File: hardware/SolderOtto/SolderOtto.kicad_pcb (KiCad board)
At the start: 2 copper layers, 102 x 80 mm, 179 parts, among them J201 Conn_02x04_Counter_Clockwise, J301 TC-2050, J401 Conn_01x20, J601 Conn_01x07, Q201 T2N7002AK, Q202 BC858B, Q203 BC847A, Q204 BC847A, Q701 BC847A, Q702 BC858B, Q703 BC847A, Q801 Q_Dual_NMOS, Q802 Q_Dual_NMOS, Q803 DTD123EK, Q804 DTD123EK, Q805 Q_Dual_NMOS, Q806 Q_Dual_NMOS, Q807 DTD123EK, Q808 DTD123EK, U201 LM5012, U202 AP3211K, U203 AP3211K, U204 AP3211K, U205 LM27761, U206 MCP9701T-E/TT, U301 STM32L496RGTx, U501 SN74LVC2G125, U701 OP07, U702 LM358, U703 74hc4053, U704 OP07, U705 OP07, U801 VOM1271, U802 VOM1271, U803 VOM1271, U804 VOM1271, Y301 Crystal

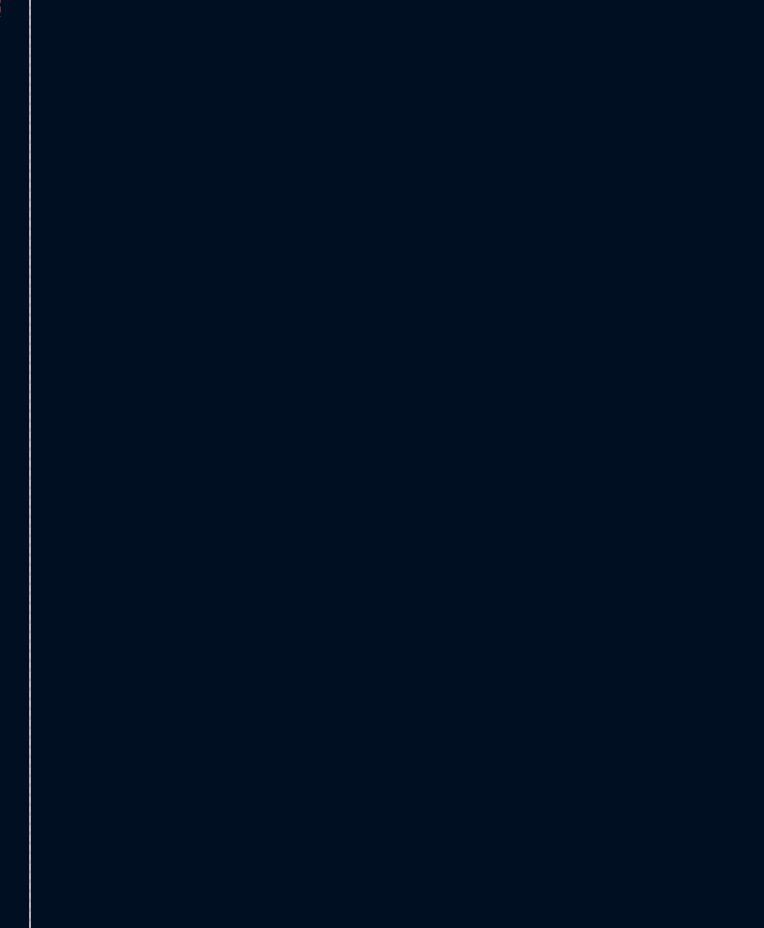
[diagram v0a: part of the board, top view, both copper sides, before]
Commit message: add support for tweezers AM-120
change mcu to stm32h573VI
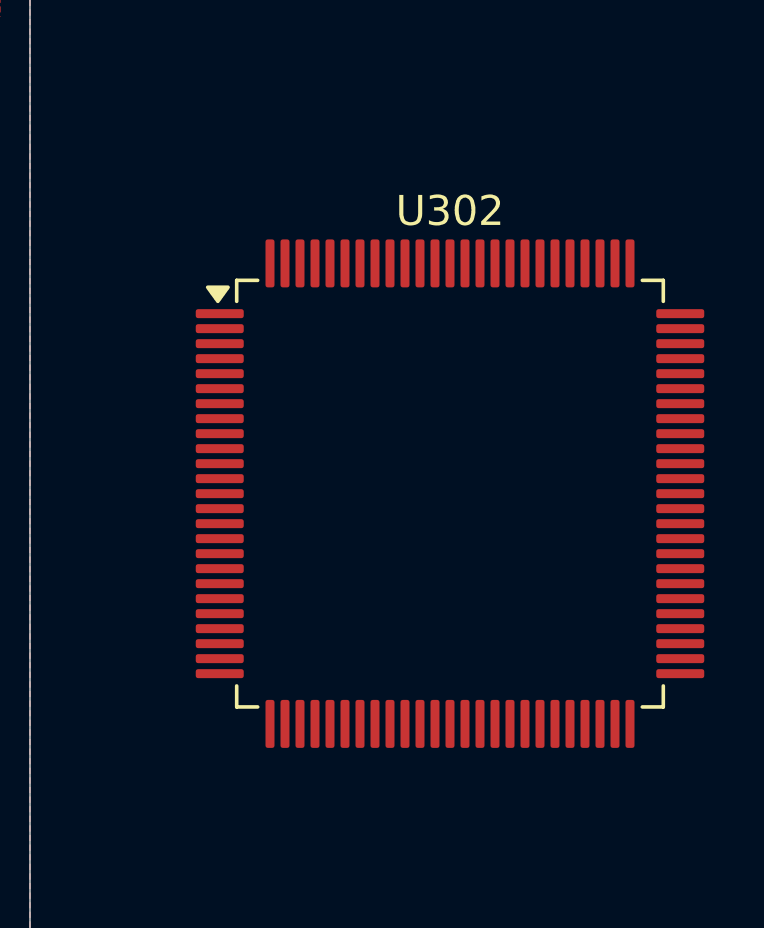
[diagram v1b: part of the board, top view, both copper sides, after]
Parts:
- added U302: STM32H573VITx, Package_QFP:LQFP-100_14x14mm_P0.5mm, F.Cu at (196.0, 105.5)

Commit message: save wip
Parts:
- removed C305, C306: 18p, Capacitor_SMD:C_0603_1608Metric
- removed U501: SN74LVC2G125, Package_SO:VSSOP-8_2.3x2mm_P0.5mm
- removed Y301: Crystal, Crystal:Crystal_SMD_0603-2Pin_6.0x3.5mm
- added C401: 100n, Capacitor_SMD:C_0603_1608Metric, F.Cu at (194.6, 55.1)
- added C402: 100n, Capacitor_SMD:C_0603_1608Metric, F.Cu at (194.6, 57.6)
- added C403: 4u7, Capacitor_SMD:C_0603_1608Metric, F.Cu at (194.6, 60.2)
- added C404: 100n, Capacitor_SMD:C_0603_1608Metric, F.Cu at (194.6, 62.7)
- added C405: 2u2, Capacitor_SMD:C_0603_1608Metric, F.Cu at (194.6, 65.2)
- added C406: 2u2, Capacitor_SMD:C_0603_1608Metric, F.Cu at (194.6, 67.7)
- added C408: 100n, Capacitor_SMD:C_0603_1608Metric, F.Cu at (194.6, 70.2)
- added C409: 100n, Capacitor_SMD:C_0603_1608Metric, F.Cu at (194.6, 72.7)
- added P401: USB_C_Plug_USB2.0, mylib_connector:USB_C_Receptacle_Molex_C_24P_SMD_RA, F.Cu at (202.4, 55.5)
- added R401: 47R, Resistor_SMD:R_0603_1608Metric, F.Cu at (194.6, 75.2)
- added R805: 11k3, Resistor_SMD:R_0603_1608Metric, F.Cu at (212.3, 60.7)
- added R806: 22k6, Resistor_SMD:R_0603_1608Metric, F.Cu at (212.3, 63.2)
- added U601: SN74LVC2G125, Package_SO:VSSOP-8_2.3x2mm_P0.5mm, F.Cu at (213.4, 55.7)
- added X401: 25MHz, Oscillator:Oscillator_SMD_SeikoEpson_SG210-4Pin_2.5x2.0mm, F.Cu at (198.8, 65.9)
- R706, R708: value 22k6 -> 11k3
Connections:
- J601 pad 3: /Channel1/_stand_sense0 -> /Channel1/_stand_sense1
- J601 pad 5: /Channel1/_stand_sense1 -> /Channel1/_stand_sense0
- Q801 pad 5: /Channel1/LOAD -> /Channel1/channel_power/LOAD0
- Q801 pad 6: /Channel1/LOAD -> /Channel1/channel_power/LOAD0
- Q803 pad 1: /Channel1/LOAD_SW_HIGH -> /Channel1/channel_power/LOAD_SW_HIGH
- Q804 pad 1: /Channel1/COM_SW_HIGH -> /Channel1/channel_power/COM_SW_HIGH
- Q805 pad 7: /Channel1/LOAD -> /Channel1/channel_power/LOAD0
- Q805 pad 8: /Channel1/LOAD -> /Channel1/channel_power/LOAD0
- R704 pad 1: /Channel1/LOAD -> /Channel1/COM
- R706 pad 1: /Channel1/COM -> /Channel1/LOAD
- R720 pad 1: Net-(R717-Pad2) -> Net-(U702A--)
- R720 pad 2: Net-(U702A--) -> Net-(R717-Pad2)
- U301 pad 38: /Channel1/COM_SW_LOW -> /mcu/Channel0_COM_L
- U301 pad 39: /Channel1/LOAD_SW_LOW -> /mcu/Channel0_LOAD_L
- U302 pad 10: Net-(U302-VSS-Pad10) -> GND
- U302 pad 100: unconnected-(U302-VDD-Pad100) -> +3V3
- U302 pad 11: unconnected-(U302-VDD-Pad11) -> +3V3
- U302 pad 14: unconnected-(U302-NRST-Pad14) -> /mcu/~{RESET}
- U302 pad 19: unconnected-(U302-VSSA-Pad19) -> GND
- U302 pad 20: unconnected-(U302-VREF--Pad20) -> GND
- U302 pad 21: unconnected-(U302-VREF+-Pad21) -> VDD_REF
- U302 pad 22: unconnected-(U302-VDDA-Pad22) -> +3V3
- U302 pad 27: Net-(U302-VSS-Pad10) -> GND
- U302 pad 28: unconnected-(U302-VDD-Pad28) -> +3V3
- U302 pad 48: unconnected-(U302-VCAP-Pad48) -> Net-(C406-Pad1)
- U302 pad 49: Net-(U302-VSS-Pad10) -> GND
- U302 pad 50: unconnected-(U302-VDD-Pad50) -> +3V3
- U302 pad 6: unconnected-(U302-VBAT-Pad6) -> +3V3
- U302 pad 73: unconnected-(U302-VDDUSB-Pad73) -> +3V3
- U302 pad 74: Net-(U302-VSS-Pad10) -> GND
- U302 pad 75: unconnected-(U302-VDD-Pad75) -> +3V3
- U302 pad 98: unconnected-(U302-VCAP-Pad98) -> Net-(C405-Pad1)
- U302 pad 99: Net-(U302-VSS-Pad10) -> GND
- U703 pad 11: unconnected-(U703-1S-Pad11) -> /Channel1/channel_meas/SEL1
- U703 pad 12: unconnected-(U703-1Y0-Pad12) -> Net-(U703-1Y0)
- U703 pad 13: unconnected-(U703-1Y1-Pad13) -> Net-(U703-1Y1)
- U703 pad 14: unconnected-(U703-1Z-Pad14) -> Net-(U701-+)
- U703 pad 15: Net-(U701-+) -> /Channel1/channel_meas/aaa
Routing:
- net /Channel1/channel_power/COM_SW_HIGH: track 0.00 -> 55.9 mm, vias 0 -> 2
- net /Channel1/COM_SW_HIGH: track 55.9 -> 0.00 mm, vias 2 -> 0
- net /Channel1/channel_power/LOAD_SW_HIGH: track 0.00 -> 53.7 mm, vias 0 -> 2
- net /Channel1/LOAD_SW_HIGH: track 53.7 -> 0.00 mm, vias 2 -> 0
- net /Channel1/LOAD: track 35.1 -> 1.84 mm, vias 21 -> 11
- net /Channel1/COM: track 41.3 -> 74.6 mm, vias 20 -> 30
- net GND: vias 373 -> 58

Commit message: wip
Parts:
- removed C402, C408, C409: 100n, Capacitor_SMD:C_0603_1608Metric
- removed C405, C406: 2u2, Capacitor_SMD:C_0603_1608Metric
- removed R401: 47R, Resistor_SMD:R_0603_1608Metric
- removed U601: SN74LVC2G125, Package_SO:VSSOP-8_2.3x2mm_P0.5mm
- removed X401: 25MHz, Oscillator:Oscillator_SMD_SeikoEpson_SG210-4Pin_2.5x2.0mm
- added BT201: Battery_Cell, Battery:BatteryHolder_LINX_BAT-HLD-012-SMT, F.Cu at (247.2, 108.5)
- added C305: 10n, Capacitor_SMD:C_0603_1608Metric, F.Cu at (219.2, 96.0)
- added C306: 1u, Capacitor_SMD:C_0603_1608Metric, F.Cu at (219.2, 98.5)
- added C307: 1u, Capacitor_SMD:C_0603_1608Metric, F.Cu at (219.2, 101.0)
- added C308: 100n, Capacitor_SMD:C_0603_1608Metric, F.Cu at (219.2, 103.5)
- added C309: 100n, Capacitor_SMD:C_0603_1608Metric, F.Cu at (255.8, 102.3)
- added C310: 9p, Capacitor_SMD:C_0603_1608Metric, F.Cu at (240.9, 118.5)
- added C311: 9p, Capacitor_SMD:C_0603_1608Metric, F.Cu at (245.8, 118.5)
- added L301: 600R@100MHz, Inductor_SMD:L_0603_1608Metric, F.Cu at (219.2, 106.0)
- added L302: 600R@100MHz, Inductor_SMD:L_0603_1608Metric, F.Cu at (219.2, 108.5)
- added Q901: Q_Dual_NMOS, Package_SO:SO-8_3.9x4.9mm_P1.27mm, F.Cu at (212.0, 83.6)
- added Q902: DTD123EK, Package_TO_SOT_SMD:SC-59, F.Cu at (218.7, 82.8)
- added R901: 470, Resistor_SMD:R_0603_1608Metric, F.Cu at (218.8, 75.7)
- added U901: VOM1271, mylib_ic:SOP-4_3.8x4.1mm_P2.54mm, F.Cu at (212.3, 77.4)
- added Y301: 32.768 kHz, Crystal:Crystal_SMD_MicroCrystal_CC8V-T1A-2Pin_2.0x1.2mm, F.Cu at (243.3, 119.3)
- D601: value BAT54SFILM -> BAS70S
- R706, R708: value 11k3 -> 20k
- R805: value 11k3 -> 2k55
- U302: value STM32H573VITx -> STM32G474VETx
- moved U302 12.1 mm to (208.0, 104.0)
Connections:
- net /Channel1/_handle_sense0 renamed /Channel1/_handle_id
- net /Channel1/_stand_sense0 renamed /Channel1/_stand_sense
- net /Channel1/_stand_sense1 renamed /Channel1/_iron_sense
- net /Channel1/channel_meas/SEL1 renamed /Channel1/SEL1
- net /Channel1/channel_meas/aaa renamed /Channel1/channel_meas/select
- D601 pad 3: /Channel1/stand_sense1 -> /Channel1/iron_sense
- D602 pad 3: /Channel1/handle_sense -> /Channel1/handle_id
- D603 pad 3: /Channel1/stand_sense0 -> /Channel1/stand_sense
- Q801 pad 5: /Channel1/channel_power/LOAD0 -> /Channel1/LOAD
- Q801 pad 6: /Channel1/channel_power/LOAD0 -> /Channel1/LOAD
- Q803 pad 1: /Channel1/channel_power/LOAD_SW_HIGH -> /Channel1/channel_power/LOAD0_SW_HIGH
- Q805 pad 7: /Channel1/channel_power/LOAD0 -> /Channel1/LOAD
- Q805 pad 8: /Channel1/channel_power/LOAD0 -> /Channel1/LOAD
- Q807 pad 1: /Channel1/LOAD_SW_LOW -> /Channel1/channel_power/LOAD_SW_LOW
- Q808 pad 1: /Channel1/COM_SW_LOW -> /Channel1/channel_power/COM_SW_LOW
- R602 pad 1: /Channel1/stand_sense1 -> /Channel1/iron_sense
- R603 pad 1: /Channel1/handle_sense -> /Channel1/handle_id
- R606 pad 1: /Channel1/stand_sense0 -> /Channel1/stand_sense
- R806 pad 1: unconnected-(R806-Pad1) -> /Channel1/channel_meas/LOAD1
- U301 pad 10: /Channel1/I_{LEAK} -> unconnected-(U301-PC2-Pad10)
- U301 pad 11: /Channel1/T_{TIP} -> unconnected-(U301-PC3-Pad11)
- U301 pad 15: /Supply/Buzzer -> unconnected-(U301-PA1-Pad15)
- U301 pad 16: /Display/QSPI_CS -> unconnected-(U301-PA2-Pad16)
- U301 pad 17: /Display/QSPI_CLK -> unconnected-(U301-PA3-Pad17)
- U301 pad 20: /Display/~{INT} -> unconnected-(U301-PA4-Pad20)
- U301 pad 21: /Display/~{PD} -> unconnected-(U301-PA5-Pad21)
- U301 pad 22: /Display/QSPI_IO3 -> unconnected-(U301-PA6-Pad22)
- U301 pad 23: /Display/QSPI_IO2 -> unconnected-(U301-PA7-Pad23)
- U301 pad 24: /Supply/T_{AMB} -> unconnected-(U301-PC4-Pad24)
- U301 pad 26: /Display/QSPI_IO1 -> unconnected-(U301-PB0-Pad26)
- U301 pad 27: /Display/QSPI_IO0 -> unconnected-(U301-PB1-Pad27)
- U301 pad 33: /Channel1/SEL2 -> unconnected-(U301-PB12-Pad33)
- U301 pad 34: /Channel1/SEL3 -> unconnected-(U301-PB13-Pad34)
- U301 pad 35: /Channel1/DET -> unconnected-(U301-PB14-Pad35)
- U301 pad 37: /mcu/Channel0_COM_H -> unconnected-(U301-PC6-Pad37)
- U301 pad 38: /mcu/Channel0_COM_L -> unconnected-(U301-PC7-Pad38)
- U301 pad 39: /mcu/Channel0_LOAD_L -> unconnected-(U301-PC8-Pad39)
- U301 pad 40: /mcu/Channel0_LOAD_H -> unconnected-(U301-PC9-Pad40)
- U301 pad 44: /Channel1/handle_sense -> unconnected-(U301-PA11-Pad44)
- U301 pad 45: /Channel1/stand_sense0 -> unconnected-(U301-PA12-Pad45)
- U301 pad 50: /Channel1/stand_sense1 -> unconnected-(U301-PA15-Pad50)
- U301 pad 51: /Channel1/tip_change -> unconnected-(U301-PC10-Pad51)
- U301 pad 54: /Supply/ZCD -> unconnected-(U301-PD2-Pad54)
- U301 pad 8: /Supply/V_{ANA} -> unconnected-(U301-PC0-Pad8)
- U301 pad 9: /Channel1/I_{LOAD} -> unconnected-(U301-PC1-Pad9)
- U302 pad 10: GND -> unconnected-(U302-PF9-Pad10)
- U302 pad 11: +3V3 -> unconnected-(U302-PF10-Pad11)
- U302 pad 14: /mcu/~{RESET} -> unconnected-(U302-PG10-Pad14)
- U302 pad 19: GND -> unconnected-(U302-PF2-Pad19)
- U302 pad 20: GND -> unconnected-(U302-PA0-Pad20)
- U302 pad 21: VDD_REF -> unconnected-(U302-PA1-Pad21)
- U302 pad 22: +3V3 -> unconnected-(U302-PA2-Pad22)
- U302 pad 23: unconnected-(U302-PA0-Pad23) -> GND
- U302 pad 24: unconnected-(U302-PA1-Pad24) -> +3V3
- U302 pad 27: GND -> unconnected-(U302-PA5-Pad27)
- U302 pad 28: +3V3 -> unconnected-(U302-PA6-Pad28)
- U302 pad 35: unconnected-(U302-PB0-Pad35) -> GND
- U302 pad 36: unconnected-(U302-PB1-Pad36) -> VDD_REF
- U302 pad 37: unconnected-(U302-PB2-Pad37) -> VDDA
- U302 pad 48: Net-(C406-Pad1) -> GND
- U302 pad 49: GND -> +3V3
- U302 pad 50: +3V3 -> unconnected-(U302-PB11-Pad50)
- U302 pad 6: +3V3 -> VBAT
- U302 pad 63: unconnected-(U302-PC6-Pad63) -> GND
- U302 pad 64: unconnected-(U302-PC7-Pad64) -> +3V3
- U302 pad 73: +3V3 -> unconnected-(U302-PA12-Pad73)
- U302 pad 98: Net-(C405-Pad1) -> unconnected-(U302-PE1-Pad98)
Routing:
- net (no net): track 0.00 -> 190.5 mm, vias 0 -> 6
- net /Channel1/COM_SW_LOW: track 67.3 -> 0.00 mm, vias 2 -> 0
- net /Channel1/LOAD_SW_LOW: track 65.1 -> 0.00 mm, vias 2 -> 0
- net /Channel1/channel_power/LOAD_SW_HIGH: track 53.7 -> 0.00 mm, vias 2 -> 0
- net /Channel1/channel_power/LOAD0_SW_HIGH: track 0.00 -> 53.7 mm, vias 0 -> 2
- net /Channel1/_iron_sense: track 36.4 -> 0.00 mm, vias 1 -> 0
- net /Channel1/stand_sense1: track 36.2 -> 0.00 mm, vias 2 -> 0
- net /Channel1/iron_sense: track 0.00 -> 36.2 mm, vias 0 -> 2
- net /Channel1/stand_sense0: track 28.6 -> 0.00 mm
- net /Channel1/stand_sense: track 0.00 -> 28.6 mm
- net /Channel1/handle_sense: track 26.4 -> 0.00 mm
- net /Channel1/handle_id: track 0.00 -> 26.4 mm
- net /Channel1/_stand_sense: track 21.6 -> 0.00 mm, vias 1 -> 0
- net unconnected-(U301-PC9-Pad40): track 0.00 -> 18.6 mm
- net /mcu/Channel0_LOAD_H: track 18.6 -> 0.00 mm
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
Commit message: save wip
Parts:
- removed BT201: Battery_Cell, Battery:BatteryHolder_LINX_BAT-HLD-012-SMT
- removed C201: 3n3, Capacitor_SMD:C_0603_1608Metric
- removed C202: 2n2, Capacitor_SMD:C_0603_1608Metric
- removed C203, C206: 47u, Capacitor_SMD:CP_Elec_10x10
- removed C204, C205: 2u2, Capacitor_SMD:C_1206_3216Metric
- removed C207: 56p, Capacitor_SMD:C_0603_1608Metric
- removed C208, C209, C210, C305: 10n, Capacitor_SMD:C_0603_1608Metric
- removed C211, C212, C213, C219: 10u, Capacitor_SMD:C_0805_2012Metric
- removed C214, C215, C216: 22u, Capacitor_SMD:C_0805_2012Metric
- removed C217, C220, C403: 4u7, Capacitor_SMD:C_0603_1608Metric
- removed C218, C221, C306, C307, C703, C704, C705, C706, C710: 1u, Capacitor_SMD:C_0603_1608Metric
- removed C301, C302, C303, C304, C308, C309, C401, C404, C601, C602, C603, C604: 100n, Capacitor_SMD:C_0603_1608Metric
- removed C310, C311: 9p, Capacitor_SMD:C_0603_1608Metric
- removed C701, C707, C708: 47p, Capacitor_SMD:C_0603_1608Metric
- removed C702, C709: 1n, Capacitor_SMD:C_0603_1608Metric
- removed C711: 100p, Capacitor_SMD:C_0603_1608Metric
- removed D201: STPS2H100A, Diode_SMD:D_SMA
- removed D202: B380B-13-F, Diode_SMD:D_SMB
- removed D203, D204, D205: SMD16PL-TP, Diode_SMD:D_SOD-123F
- removed D206, D207, D602, D603, D604, D701, D702, D703: BAT54SFILM, Package_TO_SOT_SMD:SOT-23
- removed D601: BAS70S, Package_TO_SOT_SMD:SOT-23
- removed F701: 1.25A, Fuse:Fuse_0603_1608Metric
- removed J201: Conn_02x04_Counter_Clockwise, Connector_Molex:Molex_Mini-Fit_Jr_5566-08A_2x04_P4.20mm_Vertical
- removed J301: TC-2050, mylib_connector:TC-2030
- removed J401: Conn_01x20, mylib_connector:FPC_BOTTOM_20POS_Würth_68712014522
- removed J601: Conn_01x07, Connector_Molex:Molex_Micro-Fit_3.0_43650-0715_1x07_P3.00mm_Vertical
- removed JS201: SMI-1027-T-5V-R, mylib_ic:SMI-1027-T-5V-R
- removed L201: 33u, Inductor_SMD:L_Taiyo-Yuden_NR-80xx
- removed L202: 1u5, Inductor_SMD:L_Taiyo-Yuden_NR-40xx
- removed L203, L204: 3u3, Inductor_SMD:L_Taiyo-Yuden_NR-40xx
- removed L301, L302: 600R@100MHz, Inductor_SMD:L_0603_1608Metric
- removed P401: USB_C_Plug_USB2.0, mylib_connector:USB_C_Receptacle_Molex_C_24P_SMD_RA
- removed Q201: T2N7002AK, Package_TO_SOT_SMD:SOT-23
- removed Q202, Q702: BC858B, Package_TO_SOT_SMD:SOT-23
- removed Q203, Q204, Q701, Q703: BC847A, Package_TO_SOT_SMD:SOT-23
- removed Q801, Q802, Q805, Q806, Q901: Q_Dual_NMOS, Package_SO:SO-8_3.9x4.9mm_P1.27mm
- removed Q803, Q804, Q807, Q808, Q902: DTD123EK, Package_TO_SOT_SMD:SC-59
- removed R201, R202, R721, R730: 453k, Resistor_SMD:R_0603_1608Metric
- removed R203, R221, R223: 100k, Resistor_SMD:R_0603_1608Metric
- removed R204, R205, R206, R207: 49k9, Resistor_SMD:R_0603_1608Metric
- removed R208: 5k62, Resistor_SMD:R_0603_1608Metric
- removed R209: 9k53, Resistor_SMD:R_0603_1608Metric
- removed R210: 16k2, Resistor_SMD:R_0603_1608Metric
- removed R211: 215k, Resistor_SMD:R_0603_1608Metric
- removed R212, R216, R601, R602, R603, R604, R605, R606, R607: 4k7, Resistor_SMD:R_0603_1608Metric
- removed R213: 69k, Resistor_SMD:R_0603_1608Metric
- removed R214, R217, R218, R716, R724, R731: 10k, Resistor_SMD:R_0603_1608Metric
- removed R215: 100, Resistor_SMD:R_0603_1608Metric
- removed R219: 200, Resistor_SMD:R_0603_1608Metric
- removed R220, R224, R722: 1M, Resistor_SMD:R_0603_1608Metric
- removed R222: 22k, Resistor_SMD:R_0603_1608Metric
- removed R701: 82k, Resistor_SMD:R_0603_1608Metric
- removed R702, R710: 590k, Resistor_SMD:R_0603_1608Metric
- removed R703, R704, R709, R806: 22k6, Resistor_SMD:R_0603_1608Metric
- removed R705, R711: 2k7, Resistor_SMD:R_0603_1608Metric
- removed R706, R708, R726, R729: 20k, Resistor_SMD:R_0603_1608Metric
- removed R707: 2k2, Resistor_SMD:R_0603_1608Metric
- removed R712, R723: 200k, Resistor_SMD:R_0603_1608Metric
- removed R713, R719: 4k75, Resistor_SMD:R_0603_1608Metric
- removed R714, R717, R725, R728: 3k3, Resistor_SMD:R_0603_1608Metric
- removed R715, R718: 220m, Resistor_SMD:R_0603_1608Metric
- removed R720: 187k, Resistor_SMD:R_0603_1608Metric
- removed R727: 5m, Resistor_SMD:R_Shunt_Vishay_WSKW0612
- removed R732: 470k, Resistor_SMD:R_0603_1608Metric
- removed R733, R734: 47k, Resistor_SMD:R_0603_1608Metric
- removed R801, R802, R803, R804, R901: 470, Resistor_SMD:R_0603_1608Metric
- removed R805: 2k55, Resistor_SMD:R_0603_1608Metric
- removed TP201, TP202, TP203, TP204, TP205, TP206, TP207: ZCD, TestPoint:TestPoint_Keystone_5015_Micro-Minature
- removed TP701: T_TIP, TestPoint:TestPoint_Keystone_5015_Micro-Minature
- removed TP702: I_LEAK, TestPoint:TestPoint_Keystone_5015_Micro-Minature
- removed TP703: I_LOAD, TestPoint:TestPoint_Keystone_5015_Micro-Minature
- removed TP704: DET, TestPoint:TestPoint_Keystone_5015_Micro-Minature
- removed U201: LM5012, Package_SO:TI_SO-PowerPAD-8
- removed U202, U203, U204: AP3211K, Package_TO_SOT_SMD:SOT-23-6
- removed U205: LM27761, Package_SON:WSON-8-1EP_2x2mm_P0.5mm_EP0.9x1.6mm
- removed U206: MCP9701T-E/TT, Package_TO_SOT_SMD:SOT-23-3
- removed U301: STM32L496RGTx, Package_QFP:LQFP-64_10x10mm_P0.5mm
- removed U302: STM32G474VETx, Package_QFP:LQFP-100_14x14mm_P0.5mm
- removed U701, U704, U705: OP07, Package_SO:SOIC-8_3.9x4.9mm_P1.27mm
- removed U702: LM358, Package_SO:SOIC-8_3.9x4.9mm_P1.27mm
- removed U703: 74hc4053, Package_SO:TSSOP-16_4.4x5mm_P0.65mm
- removed U801, U802, U803, U804, U901: VOM1271, mylib_ic:SOP-4_3.8x4.1mm_P2.54mm
- removed Y301: 32.768 kHz, Crystal:Crystal_SMD_MicroCrystal_CC8V-T1A-2Pin_2.0x1.2mm
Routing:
- net GND: track 352.0 -> 0.00 mm, vias 58 -> 0
- net +12V: track 308.6 -> 0.00 mm, vias 4 -> 0
- net +3V3: track 306.3 -> 0.00 mm, vias 17 -> 0
- net (no net): track 190.5 -> 0.00 mm, vias 6 -> 0
- net +8V: track 130.7 -> 0.00 mm, vias 5 -> 0
- net -5V: track 96.6 -> 0.00 mm, vias 7 -> 0
- net 24V_{AC}: track 95.2 -> 0.00 mm, vias 16 -> 0
- net /Channel1/I_{LOAD}: track 77.8 -> 0.00 mm, vias 2 -> 0
- net /Channel1/COM: track 74.6 -> 0.00 mm, vias 30 -> 0
- net +5V: track 73.4 -> 0.00 mm, vias 6 -> 0
- net Earth: track 63.6 -> 0.00 mm, vias 3 -> 0
- net /Channel1/I_{LEAK}: track 60.1 -> 0.00 mm, vias 2 -> 0
- net /Channel1/T_{TIP}: track 58.1 -> 0.00 mm, vias 2 -> 0
- net /Channel1/channel_power/COM_SW_HIGH: track 55.9 -> 0.00 mm, vias 2 -> 0
- net /Channel1/channel_power/LOAD0_SW_HIGH: track 53.7 -> 0.00 mm, vias 2 -> 0
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- removed copper zone on F.Cu, net +12V
- removed copper zone on F.Cu, net +3V3
- removed copper zone on F.Cu, net +5V
- removed copper zone on F.Cu, net +8V
- removed copper zone on F.Cu, net -5V
- removed copper zone on B.Cu, net /Channel1/COM
- removed copper zone on F.Cu, net /Channel1/COM
- removed copper zone on B.Cu, net /Channel1/LOAD
- removed copper zone on F.Cu, net /Channel1/LOAD
- removed copper zone on B.Cu, net /Channel1/channel_meas/CURRENT
- removed copper zone on F.Cu, net /Channel1/channel_meas/CURRENT
- removed copper zone on B.Cu, net 24V_{AC}
- removed copper zone on F.Cu, net 24V_{AC}
- removed copper zone on B.Cu, net GND
- removed copper zone on F.Cu, net GND
- removed copper zone on F.Cu, net Net-(D201-K)
- removed copper zone on F.Cu, net Net-(D202-K)
- removed copper zone on F.Cu, net Net-(D203-K)
- removed copper zone on F.Cu, net Net-(D204-K)
- removed copper zone on F.Cu, net Net-(D205-K)
- removed copper zone on B.Cu, net Net-(Q801A-S)
- removed copper zone on F.Cu, net Net-(Q801A-S)
- removed copper zone on B.Cu, net Net-(Q802A-S)
- removed copper zone on F.Cu, net Net-(Q802A-S)
- removed copper zone on B.Cu, net Net-(Q805A-S)
- removed copper zone on F.Cu, net Net-(Q805A-S)
- removed copper zone on B.Cu, net Net-(Q806A-S)
- removed copper zone on F.Cu, net Net-(Q806A-S)
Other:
- board size 102 x 80 mm -> 165 x 70 mm
- copper layers 2 -> 4
- board text removed: "SolderOtto v0.1"
